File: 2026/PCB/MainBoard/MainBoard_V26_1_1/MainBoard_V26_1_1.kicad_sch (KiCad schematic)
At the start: 87 parts, among them J1 Raspberry_Pi_2_3, J13 //Drib, J15 TFT3, J16 CAN_CON, J2 fan, J4 metor, J6 Debug, J8 MOLEX MINISPOX, Q1 Q_NMOS_GSD, Q2 Q_NMOS_GSD, SW1 SW_MEC_5E, SW2 Ras_1, SW3 Ras_2, SW4 SW_Wuerth_450301014042, SW5 SW_MEC_5E, SW6 SW_MEC_5E, U1 STM32F446RETx, U10 MPU9250, U2 LMR51460FSQDRRRQ1, U3 MOUDLE-SEEEDUINO-XIAO, U5 MCP1703AT-3302E/CB, U6 BNO055, U8 MAX3051, Y1 CSTNE16M0V530000R0

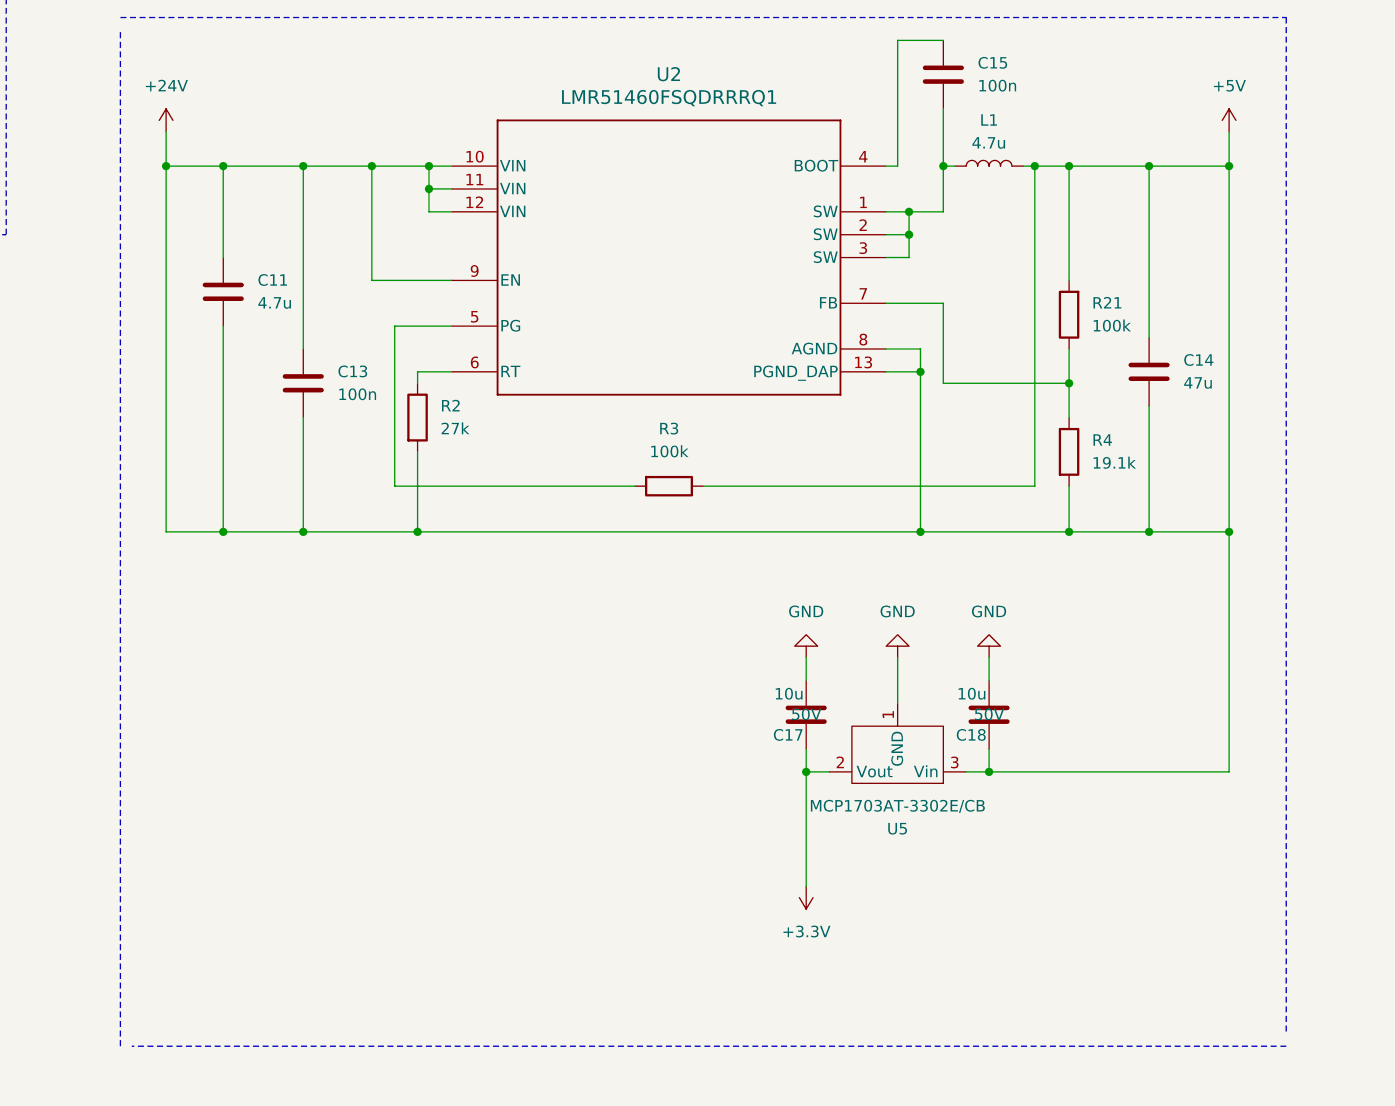
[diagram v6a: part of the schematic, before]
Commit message: PCB配線開始、コネクタ類仮配置
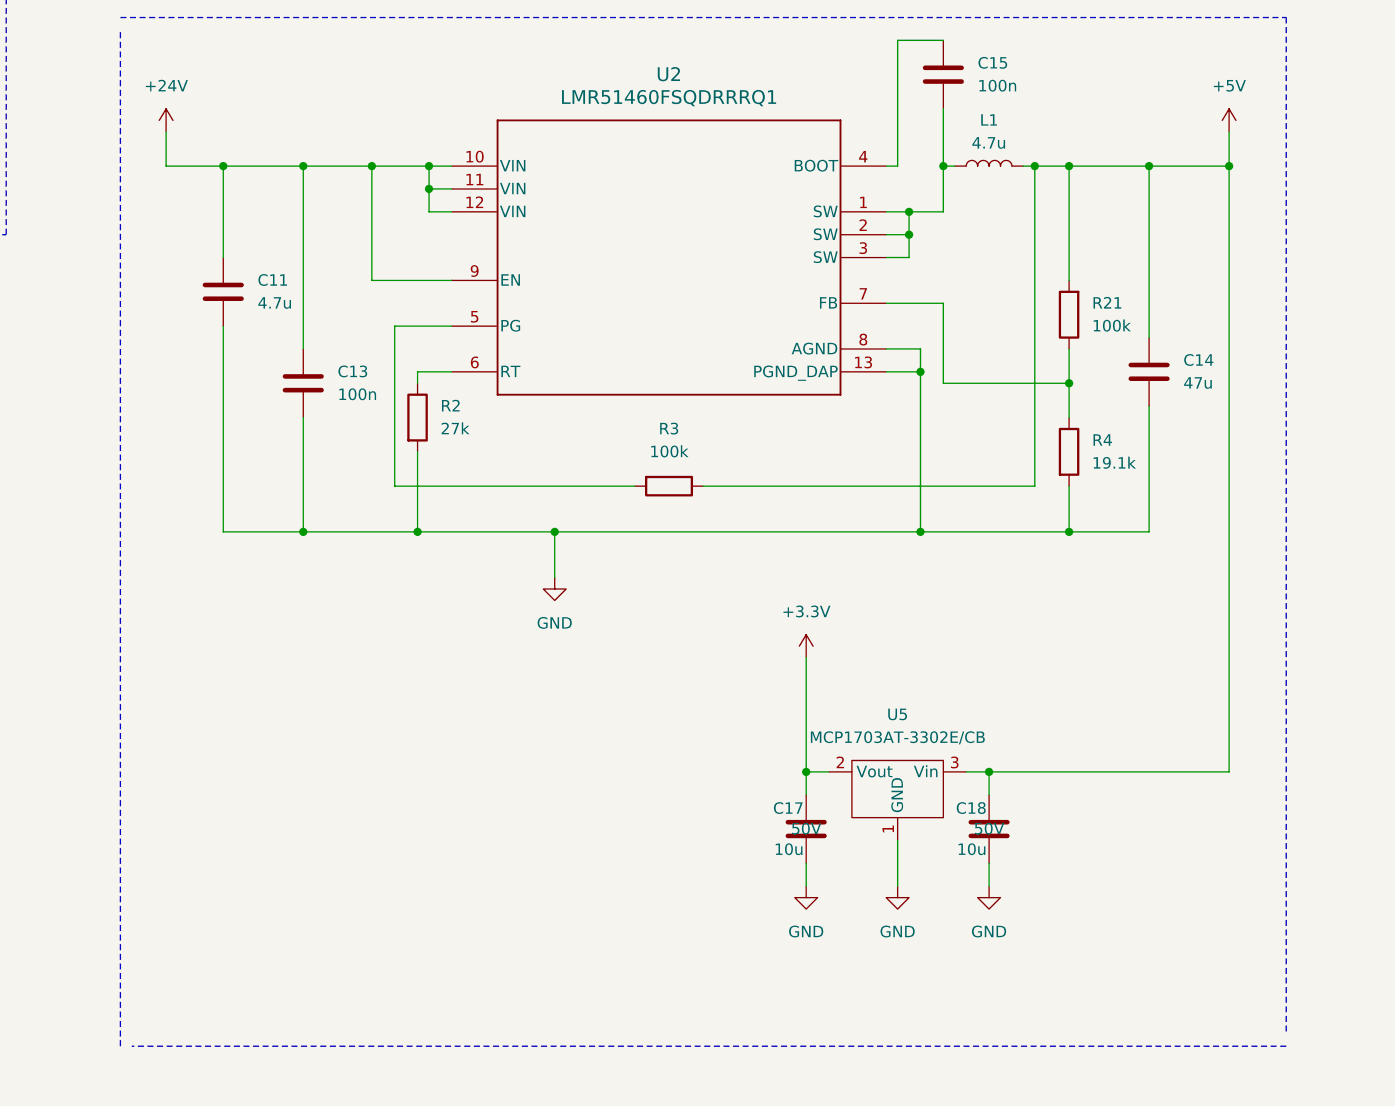
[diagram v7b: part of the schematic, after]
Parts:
- L1: footprint (none) -> 0_Library:IND_IHLP-4040DZ_VIS
- R2, R21, R3, R4: footprint (none) -> Resistor_SMD:R_0603_1608Metric_Pad0.98x0.95mm_HandSolder
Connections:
- net +24V: no longer C10.1, C11.2, C12.1, C13.2, C14.1, C14.2, C18.1, C24.1, C9.1, D3.2 (A), J1.2 (5V), J1.4 (5V), J2.1 (Pin_1), L1.2, R2.2, R21.2, R3.1, R4.2, U2.13 (PGND_DAP), U2.8 (AGND), U3.14 (5V), U5.3 (Vin)
- net GND: now also C11.2, C13.2, C14.2, R2.2, R4.2, U2.13 (PGND_DAP), U2.8 (AGND)
- new net +5V: C10.1, C12.1, C14.1, C18.1, C24.1, C9.1, D3.2 (A), J1.2 (5V), J1.4 (5V), J2.1 (Pin_1), L1.2, R21.2, R3.1, U3.14 (5V), U5.3 (Vin)
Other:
- moved on the sheet: C17, C18, U5

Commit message: 配置一旦終わり。一部仮置き
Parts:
- removed J4: metor, Resistor_SMD:R_MiniMELF_MMA-0204, symbol Connector:Conn_01x02_Pin
- removed J8: MOLEX MINISPOX, Connector_Molex:Molex_SPOX_5268-05A_1x05_P2.50mm_Horizontal, symbol Connector:Conn_01x05_Socket
- added J3: MOLEX, Connector_Molex:Molex_SPOX_5268-04A_1x04_P2.50mm_Horizontal, symbol Connector:Conn_01x04_Socket
- added J5: Conn_01x05_Socket, Connector_JST:JST_PH_S5B-PH-K_1x05_P2.00mm_Horizontal, symbol Connector:Conn_01x05_Socket
- C14: footprint (none) -> Capacitor_SMD:C_0805_2012Metric_Pad1.18x1.45mm_HandSolder
- H1, H2, H4, H5: footprint MountingHole:MountingHole_3.2mm_M3_Pad_Via -> MountingHole:MountingHole_3.2mm_M3_DIN965_Pad_TopBottom
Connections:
- net VD is gone; now on net +24V: LS1.P, R10.1, R7.1
- net +24V: now also J3.2 (Pin_2)
- net CANH: now also J3.3 (Pin_3)
- net CANL: now also J3.4 (Pin_4)
- net GND: now also J3.1 (Pin_1)
- net MD1_RX: now also J5.1 (Pin_1)
- net MD1_TX: now also J5.2 (Pin_2)
- net MD2_TX: now also J5.3 (Pin_3)
- net MD3_TX: now also J5.4 (Pin_4)
- net MD4_TX: now also J5.5 (Pin_5)
